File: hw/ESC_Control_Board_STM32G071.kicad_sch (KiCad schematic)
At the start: 5 parts, among them J2 Conn_01x03, J3 Conn_01x04, J4 Conn_01x04, J5 Conn_01x02, J6 Conn_01x15

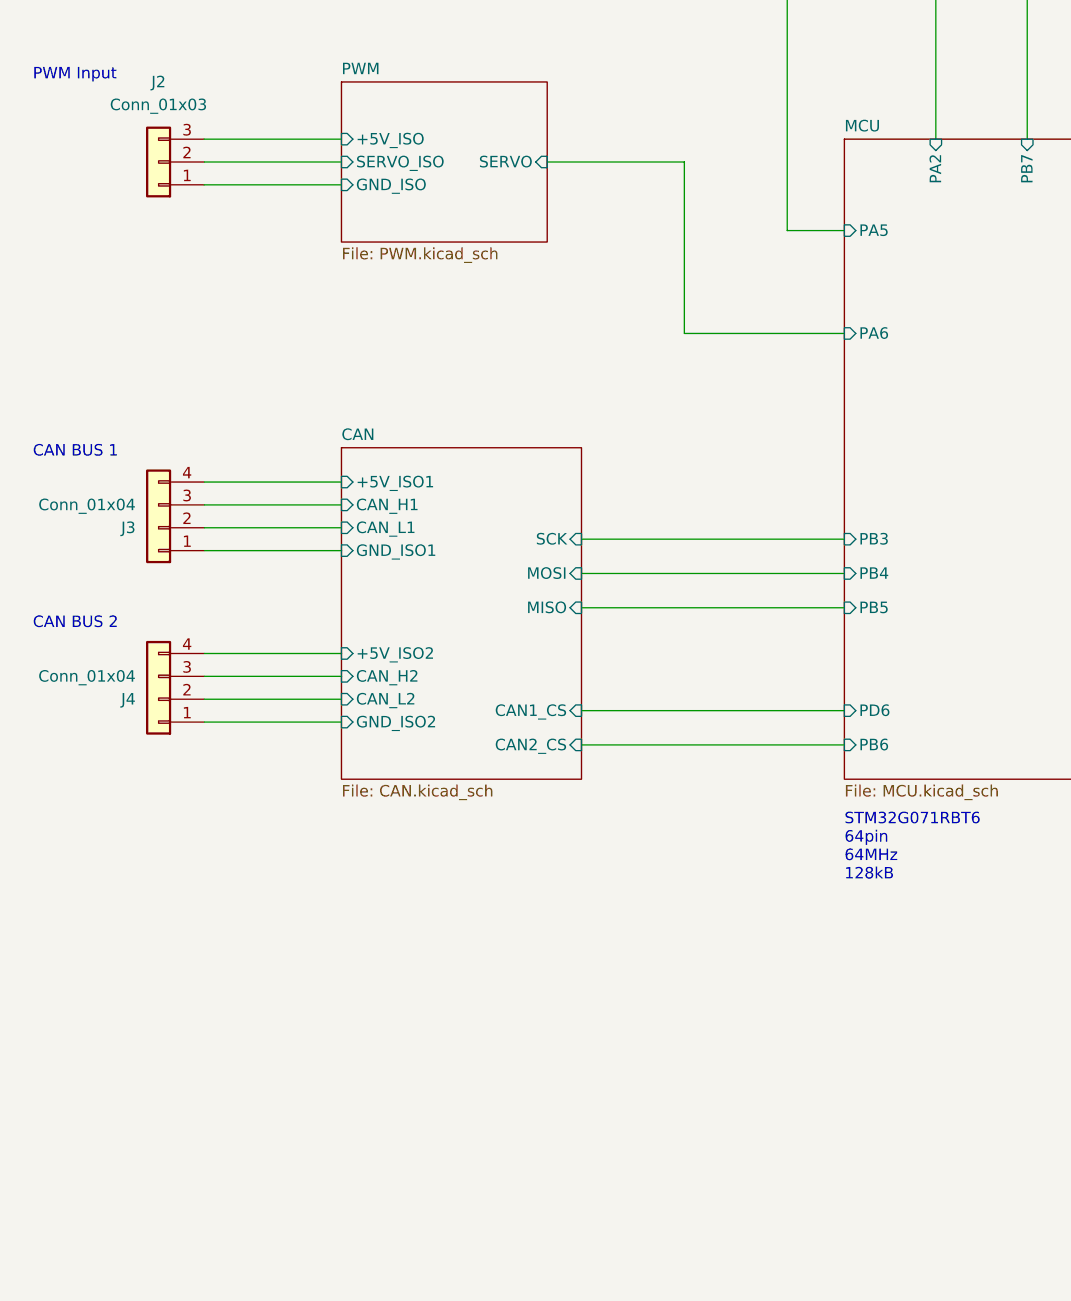
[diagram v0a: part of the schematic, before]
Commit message: connected interrupt pins to CAN controller
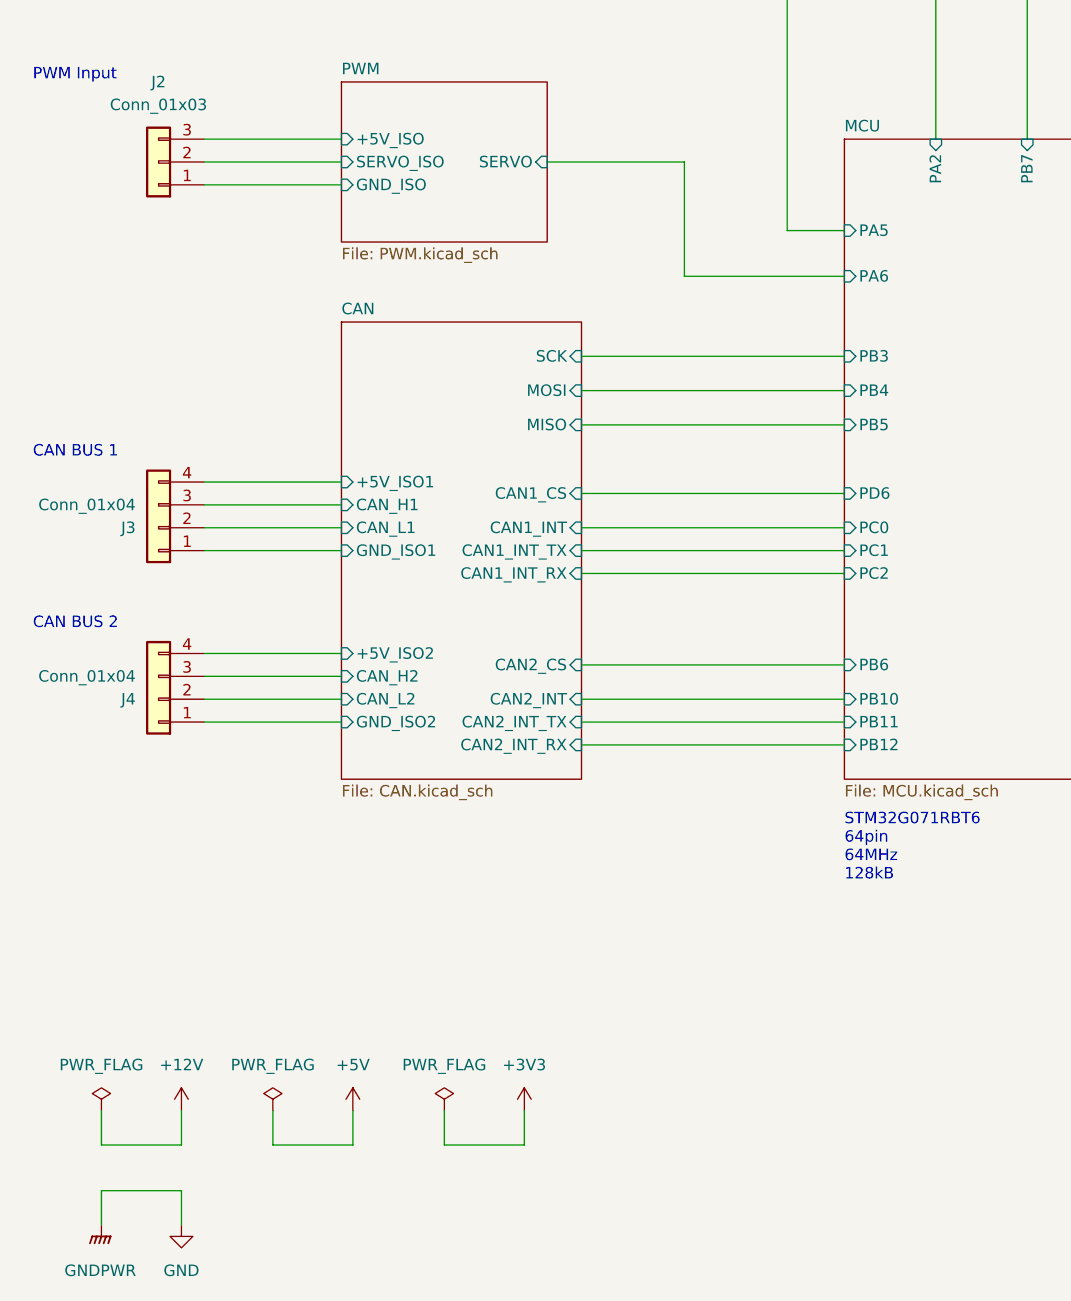
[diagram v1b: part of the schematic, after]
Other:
- sheet CAN ports: added CAN1_INT, CAN1_INT_RX, CAN1_INT_TX, CAN2_INT, CAN2_INT_RX, CAN2_INT_TX; removed none
- sheet MCU ports: added PB10, PB11, PB12, PC0, PC1, PC2; removed none
